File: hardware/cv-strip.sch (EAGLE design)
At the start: 83 parts, among them IC1 PIC16F1825SO14, IC2 74HC595D, IC3 74HC595D, IC4 MCP4728_QUAD_DAC, IC5 LM324D, IC6 REG1117, IC7 6N138

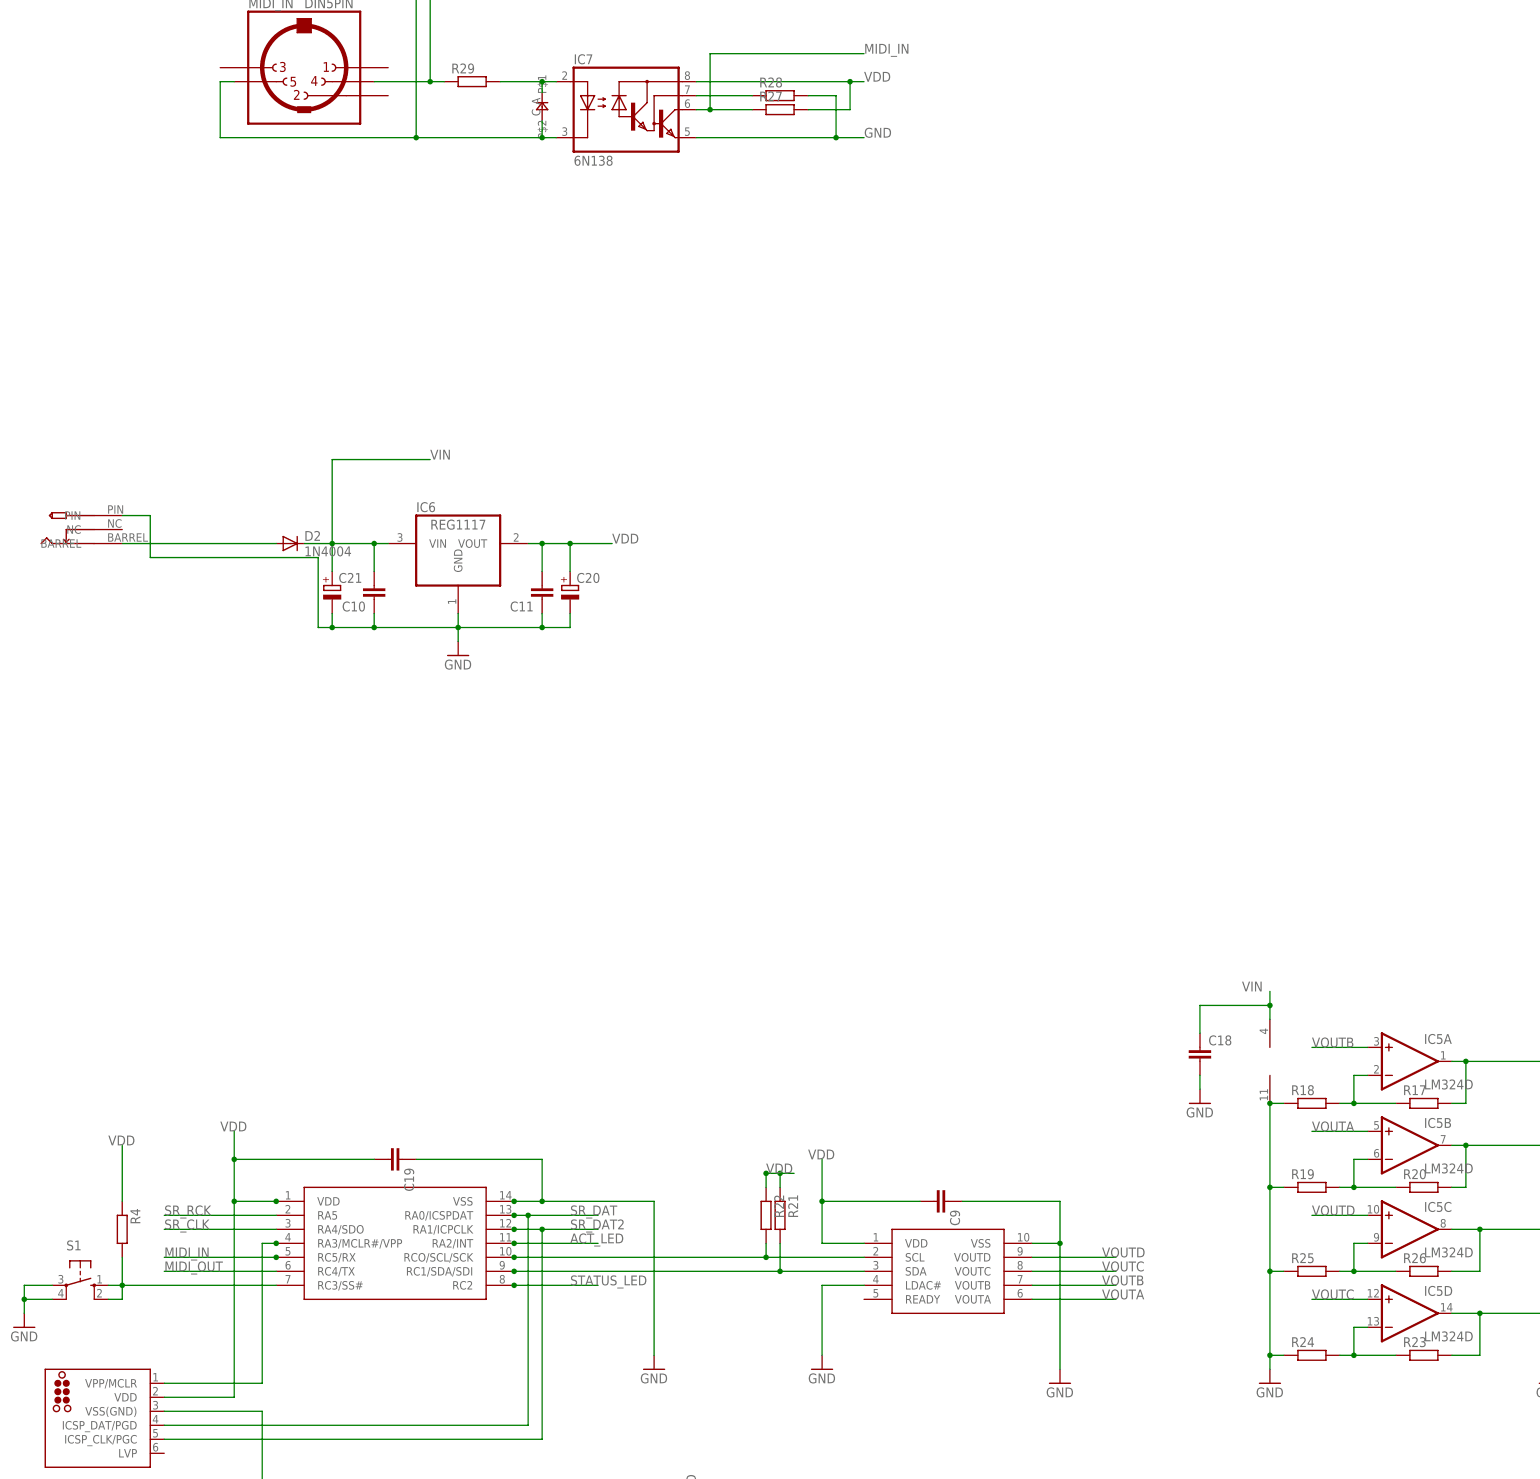
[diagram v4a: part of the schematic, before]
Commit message: add comp values
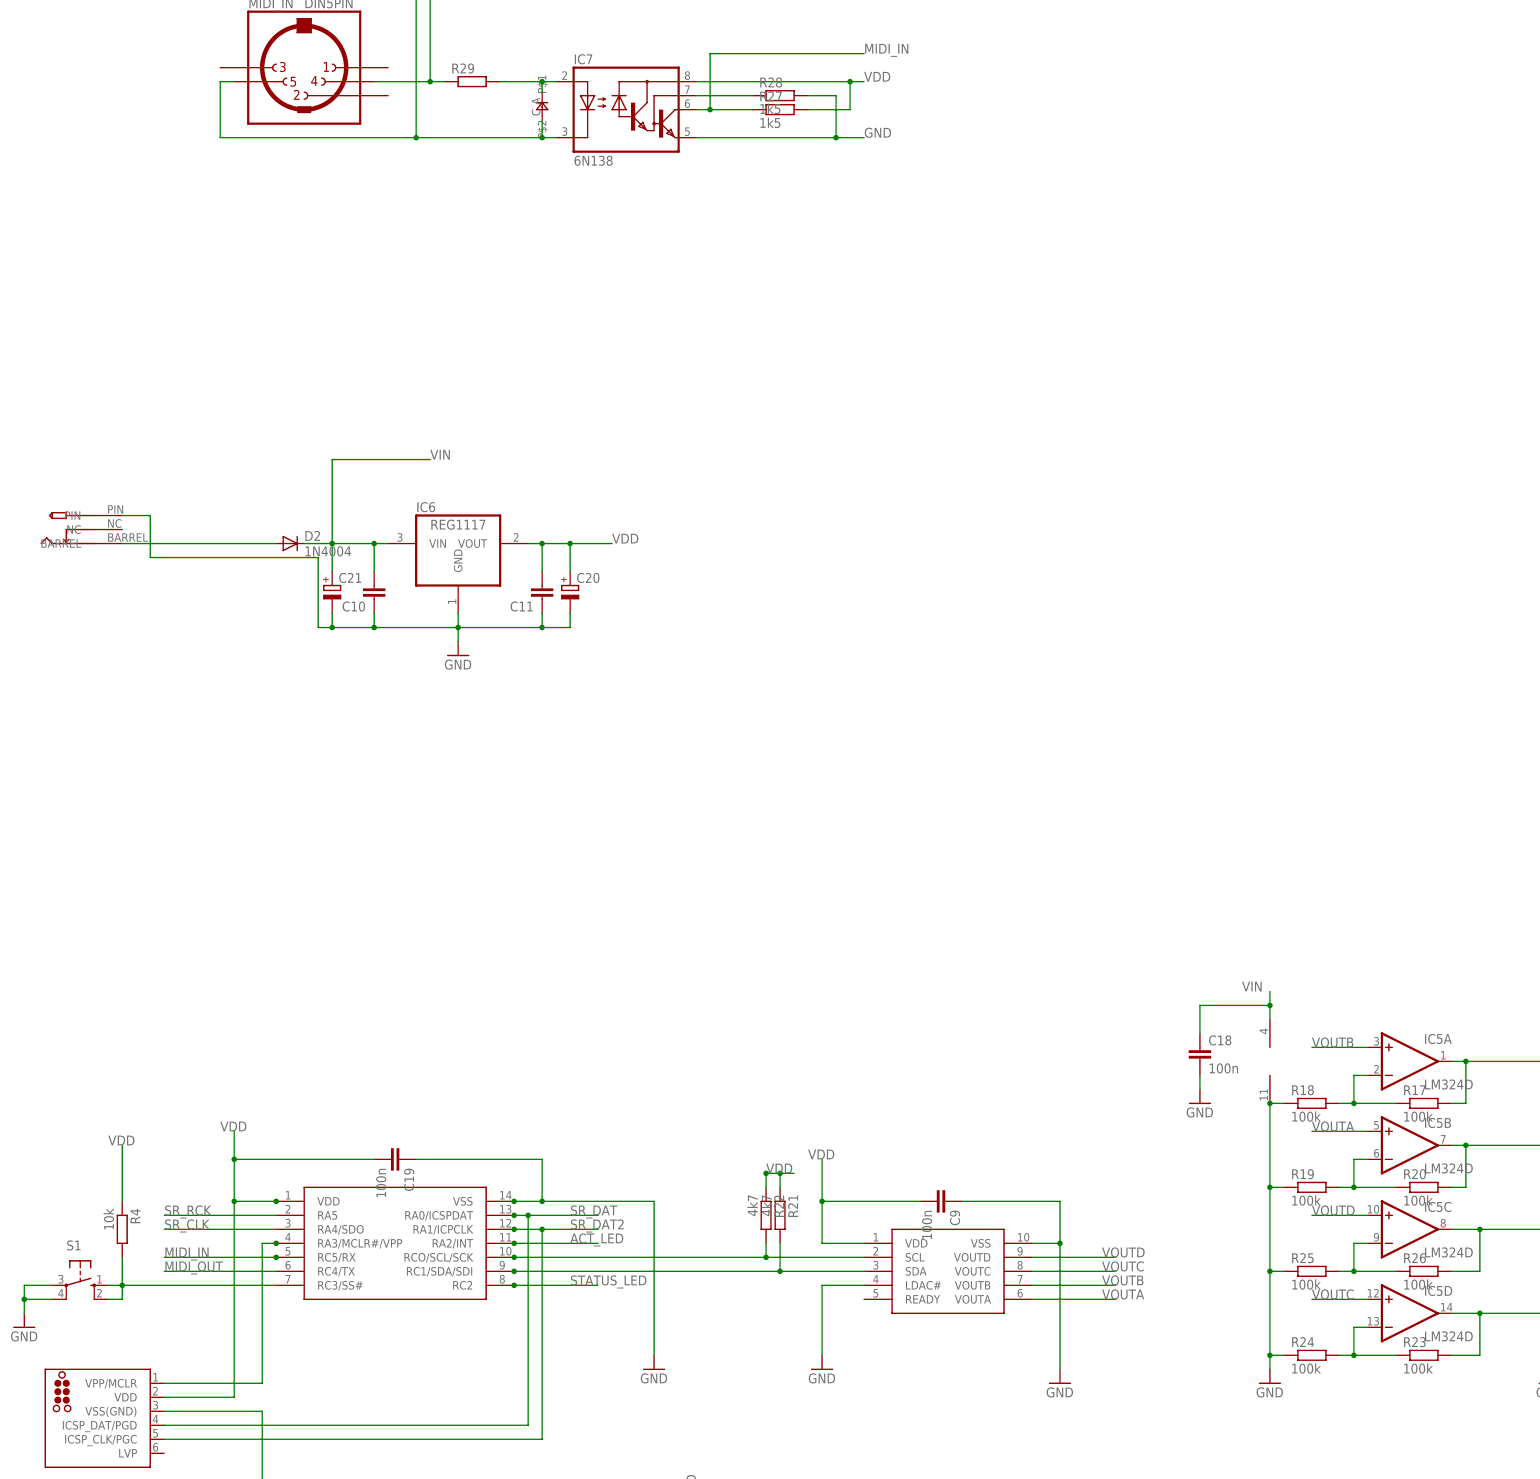
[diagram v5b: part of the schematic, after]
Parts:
- C18, C19, C9: value (none) -> 100n
- R17, R18, R19, R20, R23, R24, R25, R26: value (none) -> 100k
- R21, R22: value (none) -> 4k7
- R27, R28: value (none) -> 1k5
- R4: value (none) -> 10k
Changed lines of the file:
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@@
 <part name="R16" library="rcl" deviceset="R-EU_" device="R0805"/>
 <part name="GND2" library="supply1" deviceset="GND" device=""/>
-<part name="R22" library="rcl" deviceset="R-EU_" device="R0805"/>
-<part name="R21" library="rcl" deviceset="R-EU_" device="R0805"/>
+<part name="R22" library="rcl" deviceset="R-EU_" device="R0805" value="4k7"/>
+<part name="R21" library="rcl" deviceset="R-EU_" device="R0805" value="4k7"/>
 <part name="GND12" library="supply1" deviceset="GND" device=""/>
 <part name="IC5" library="linear" deviceset="LM324" device="D"/>
-<part name="R17" library="rcl" deviceset="R-EU_" device="R0805"/>
-<part name="R20" library="rcl" deviceset="R-EU_" device="R0805"/>
-<part name="R26" library="rcl" deviceset="R-EU_" device="R0805"/>
-<part name="R23" library="rcl" deviceset="R-EU_" device="R0805"/>
-<part name="R18" library="rcl" deviceset="R-EU_" device="R0805"/>
-<part name="R19" library="rcl" deviceset="R-EU_" device="R0805"/>
-<part name="R25" library="rcl" deviceset="R-EU_" device="R0805"/>
-<part name="R24" library="rcl" deviceset="R-EU_" device="R0805"/>
+<part name="R17" library="rcl" deviceset="R-EU_" device="R0805" value="100k"/>
+<part name="R20" library="rcl" deviceset="R-EU_" device="R0805" value="100k"/>
+<part name="R26" library="rcl" deviceset="R-EU_" device="R0805" value="100k"/>
+<part name="R23" library="rcl" deviceset="R-EU_" device="R0805" value="100k"/>
+<part name="R18" library="rcl" deviceset="R-EU_" device="R0805" value="100k"/>
+<part name="R19" library="rcl" deviceset="R-EU_" device="R0805" value="100k"/>
+<part name="R25" library="rcl" deviceset="R-EU_" device="R0805" value="100k"/>
+<part name="R24" library="rcl" deviceset="R-EU_" device="R0805" value="100k"/>
 <part name="GND1" library="supply1" deviceset="GND" device=""/>
 <part name="GND13" library="supply1" deviceset="GND" device=""/>
@@
 <part name="C13" library="rcl" deviceset="C-EU" device="C0805"/>
 <part name="GND15" library="supply1" deviceset="GND" device=""/>
-<part name="C9" library="rcl" deviceset="C-EU" device="C0805"/>
-<part name="C19" library="rcl" deviceset="C-EU" device="C0805"/>
+<part name="C9" library="rcl" deviceset="C-EU" device="C0805" value="100n"/>
+<part name="C19" library="rcl" deviceset="C-EU" device="C0805" value="100n"/>
 <part name="C17" library="rcl" deviceset="C-EU" device="C0805"/>
 <part name="C15" library="rcl" deviceset="C-EU" device="C0805"/>
@@
 <part name="R29" library="rcl" deviceset="R-EU_" device="R0805"/>
 <part name="D1" library="jasons_stuff" deviceset="0805DIODE" device=""/>
-<part name="R27" library="rcl" deviceset="R-EU_" device="R0805"/>
-<part name="R28" library="rcl" deviceset="R-EU_" device="R0805"/>
+<part name="R27" library="rcl" deviceset="R-EU_" device="R0805" value="1k5"/>
+<part name="R28" library="rcl" deviceset="R-EU_" device="R0805" value="1k5"/>
 <part name="DRM1" library="jason_eagle6" deviceset="VERTICAL_3_5MM_SOCKET" device=""/>
 <part name="DRM2" library="jason_eagle6" deviceset="VERTICAL_3_5MM_SOCKET" device=""/>
@@
 <part name="C20" library="resistor" deviceset="CPOL-EU" device="E2.5-5"/>
 <part name="S1" library="switch-omron" deviceset="10-XX" device=""/>
-<part name="R4" library="rcl" deviceset="R-EU_" device="R0805"/>
+<part name="R4" library="rcl" deviceset="R-EU_" device="R0805" value="10k"/>
 <part name="GND7" library="supply1" deviceset="GND" device=""/>
-<part name="C18" library="rcl" deviceset="C-EU" device="C0805"/>
+<part name="C18" library="rcl" deviceset="C-EU" device="C0805" value="100n"/>
 <part name="GND8" library="supply1" deviceset="GND" device=""/>
 <part name="U$2" library="jason_eagle6" deviceset="PWR_SOCKET_2_1MM" device=""/>

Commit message: rev2 updates - checking needed
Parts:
- removed D2: 1N4004, jasons_stuff:1N4004
- removed L1, L2, L3: (no value), led:LED3MM
- added ACT, PWR, STA: (no value), led:LED3MM
- added C22: (no value), microbuilder:CAP_TANTALUMA/3216_REFLOW
- added D3, D4, D5: (no value), microbuilder:DIODESOD-123
- added Q1, Q2, Q4: (no value), microbuilder:MOSFET-N_DUAL
- added Q3, Q5: (no value), microbuilder:MOSFET-P
- added R30, R31, R32, R33, R34, R35, R36, R37, R38, R39: (no value), rcl:R-EU_R0805
- IC2: value 74HC595D -> AD5696R; device 74xx-eu:74HC595D -> jason_eagle6:AD5696R
- IC3: value 74HC595D -> MC14094B; device 74xx-eu:74HC595D -> jason_eagle6:MC14094B
- IC4: value MCP4728_QUAD_DAC -> MC14094B; device jason_eagle6:MCP4728_QUAD_DAC -> jason_eagle6:MC14094B
- renumbered CLK1 to GT2, CLK2 to GT4, DRM1 to GT9, DRM2 to GT10, DRM3 to GT11, DRM4 to GT8, DRM5 to GT5, DRM6 to GT6, DRM7 to GT7, DRM8 to GT12, GATE1 to GT1, GATE2 to GT3, NOTE1CV to CVC, NOTE2CV to CVA, S1 to MODE, VEL1CV to CVB, VEL2CV to CVD
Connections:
- removed net MIDI_OUT: IC1.RC4/TX
- removed net N$22: IC1.RC1/SDA/SDI, IC4.SDA, R21.2
- removed net N$47: IC2A.QD, R5.1
- removed net N$51: IC2A.QE, R12.1
- removed net N$53: IC2A.QH, R9.1
- new net GT1_VSEL: IC1.RC4/TX, R38.1
- new net GT2_VSEL: IC1.RC3/SS#, R39.1
- new net N$10: IC3.Q2, R15.1
- new net N$11: IC3.Q4, R16.1
- new net N$14: IC3.STROBE, Q1G$1.D, R31.1
- new net N$17: IC4.Q8, R9.1
- new net N$18: IC4.Q7, R10.1
- new net N$19: IC4.Q6, R11.1
- new net N$38: IC4.Q5, R12.1
- new net N$44: IC4.Q3, R6.1
- new net N$45: IC4.Q2, R7.1
- new net SCL: IC1.RCO/SCL/SCK, IC2.SCL, R22.2
- new net SDA: IC1.RC1/SDA/SDI, IC2.SDA, R21.2
- new net VDD_GT1: C13.1, D3.C, IC3.OE, IC3.VDD, Q3.D, R30.2, R31.2, R32.2
- new net VDD_GT2: C12.1, D4.C, IC4.OE, IC4.VDD, Q5.D, R33.2, R34.2, R35.2
- net ACT_LED: now also ACT.A; no longer L1.A
- net GND: now also C22.-, C9.2, IC2.A0, IC2.A1, IC2.GND, IC2.LDAC#, IC2.RSTSEL, IC3.VSS, Q1G$1.S, Q1G$2.S, Q2G$1.S, Q2G$2.S, Q4G$1.S, Q4G$2.S; no longer C9.1, IC2A.G, IC2P.GND, IC3A.G, IC3P.GND, IC4.LDAC#
- net N$12: now also IC3.Q3, R14.1; no longer IC3A.QA, R15.1
- net N$13: now also IC3.Q1, R13.1; no longer IC3A.QB, R16.1
- net N$15: now also IC3.DATA, Q1G$2.D, R30.1; no longer IC3A.QD, R13.1
- net N$16: now also IC3.CLOCK, Q2G$2.D, R32.1; no longer IC3A.QC, R14.1
- net N$21: now also Q5.G, R37.1, R39.2; no longer IC1.RCO/SCL/SCK, IC4.SCL, R22.2
- net N$34: now also MODE.S, MODE.S1, R4.2
- net N$35: now also PWR.C; no longer L3.C
- net N$36: now also ACT.C; no longer L1.C
- net N$37: now also STA.C; no longer L2.C
- net N$40: now also D5.A; no longer D2.A
- net N$43: now also IC4.Q4, R5.1; no longer IC2A.QA, R8.1
- net N$46: now also IC4.Q1, R8.1; no longer IC2A.QB, R7.1
- net N$48: now also IC4.STROBE, Q2G$1.D, R33.1; no longer IC2A.QC, R6.1
- net N$49: now also IC4.DATA, Q4G$1.D, R34.1; no longer IC2A.QF, R11.1
- net N$50: now also IC4.CLOCK, Q4G$2.D, R35.1; no longer IC2A.QG, R10.1
- net N$9: now also Q3.G, R36.1, R38.2; no longer IC1.RC3/SS#, MODE.S, MODE.S1, R4.2
- net SR_CLK: now also Q2G$2.G, Q4G$2.G; no longer IC2A.SCK, IC3A.SCK
- net SR_DAT: now also Q1G$2.G; no longer IC3A.SER
- net SR_DAT2: now also Q4G$1.G; no longer IC2A.SER
- net SR_RCK: now also Q1G$1.G, Q2G$1.G; no longer IC2A.RCK, IC3A.RCK
- net STATUS_LED: now also STA.A; no longer L2.A
- net VDD: now also C22.+, C9.1, D3.A, D4.A, IC2.GAIN, IC2.RESET#, IC2.VDD, IC2.VLOGIC, PWR.A; no longer C12.1, C13.1, C9.2, IC2A.SCL, IC2P.VCC, IC3A.SCL, IC3P.VCC, IC4.VDD, L3.A
- net VIN: now also D5.C, Q3.S, Q5.S, R36.2, R37.2; no longer D2.C
- net VOUTA: now also IC2.VOUTA, IC5A.+IN; no longer IC4.VOUTA, IC5B.+IN
- net VOUTB: now also IC2.VOUTB, IC5B.+IN; no longer IC4.VOUTB, IC5A.+IN
- net VOUTC: now also IC2.VOUTC; no longer IC4.VOUTC
- net VOUTD: now also IC2.VOUTD; no longer IC4.VOUTD
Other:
- note added: "CV OUTPUT 16-BIT DAC"
- note added: "CV OUTPUT BUFFERS"
- note added: "GATES 1-4 DRIVE"
- note added: "GATES 5-12 DRIVE"
- note added: "GATES VOLTAGE LEVEL SELECT"
- note added: "LEVEL SHIFT"
- note added: "MIDI DATA INPUT"
- note added: "MIDI-TO-CV CONVERTER JASON HOTCHKISS SIXTY FOUR PIXELS LTD 29 MAY 2016"
- note added: "PIC16F1825 MICRO CONTROLLER"
- note added: "POWER SUPPLY REGULATOR"
- moved on the sheet: C10, C11, C12, C13, C20, C21, C9, IC6, IC7, MIDI, MIDI_IN, R1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
